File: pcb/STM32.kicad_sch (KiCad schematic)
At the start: 4 parts, among them CN1 Conn_02x08_Odd_Even, CN2 Conn_02x15_Odd_Even, CN3 Conn_02x10_Odd_Even, CN4 Conn_02x17_Odd_Even

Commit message: Updated PCB
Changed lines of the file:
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@@
 (kicad_sch (version 20230121) (generator eeschema)
   (paper "A4")
+  (hierarchical_label "Endschalter_Hinten_MCU" (shape input) (at 72.39 105.41 180) (fields_autoplaced)
+    (effects (font (size 1.27 1.27)) (justify right))
+  )
+  (hierarchical_label "Abstandsmessung_MCU" (shape input) (at 72.39 82.55 180) (fields_autoplaced)
+    (effects (font (size 1.27 1.27)) (justify right))
+  )
+  (hierarchical_label "Windgeschwindigkeit_MCU" (shape input) (at 72.39 74.93 180) (fields_autoplaced)
+    (effects (font (size 1.27 1.27)) (justify right))
+  )
+  (hierarchical_label "IN2_MCU" (shape output) (at 72.39 93.98 180) (fields_autoplaced)
+    (effects (font (size 1.27 1.27)) (justify right))
+  )
+  (hierarchical_label "IN1_MCU" (shape output) (at 72.39 90.17 180) (fields_autoplaced)
+    (effects (font (size 1.27 1.27)) (justify right))
+  )
+  (hierarchical_label "IN3_MCU" (shape output) (at 72.39 97.79 180) (fields_autoplaced)
+    (effects (font (size 1.27 1.27)) (justify right))
+  )
+  (hierarchical_label "Endschalter_Vorne_MCU" (shape input) (at 72.39 101.6 180) (fields_autoplaced)
+    (effects (font (size 1.27 1.27)) (justify right))
+  )
+  (hierarchical_label "Windrichtung_MCU" (shape input) (at 72.39 78.74 180) (fields_autoplaced)
+    (effects (font (size 1.27 1.27)) (justify right))
+  )
+  (hierarchical_label "Drehzahl_Analog_OUT" (shape input) (at 72.39 109.22 180) (fields_autoplaced)
+    (effects (font (size 1.27 1.27)) (justify right))
+  )
+  (hierarchical_label "IN0_MCU" (shape output) (at 72.39 86.36 180) (fields_autoplaced)
+    (effects (font (size 1.27 1.27)) (justify right))
+  )
+  (hierarchical_label "Kraftmessung_MCU" (shape input) (at 72.39 71.12 180) (fields_autoplaced)
+    (effects (font (size 1.27 1.27)) (justify right))
+  )
   (symbol (lib_id "Connector_Generic:Conn_02x17_Odd_Even") (at 166.37 100.33 0) (unit 1)
     (in_bom yes) (on_board yes) (dnp no) (fields_autoplaced)

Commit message: updated pcb
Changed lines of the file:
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@@
+    (effects (font (size 1.27 1.27)) (justify right))
+  )
+  (hierarchical_label "UART_EN" (shape output) (at 72.39 129.54 180) (fields_autoplaced)
     (effects (font (size 1.27 1.27)) (justify right))
   )
   (hierarchical_label "Windgeschwindigkeit_MCU" (shape input) (at 72.39 74.93 180) (fields_autoplaced)
+    (effects (font (size 1.27 1.27)) (justify right))
+  )
+  (hierarchical_label "OUT2_MCU" (shape output) (at 72.39 116.84 180) (fields_autoplaced)
+    (effects (font (size 1.27 1.27)) (justify right))
+  )
+  (hierarchical_label "UART_RX" (shape input) (at 72.39 124.46 180) (fields_autoplaced)
     (effects (font (size 1.27 1.27)) (justify right))
   )
@@
     (effects (font (size 1.27 1.27)) (justify right))
   )
+  (hierarchical_label "OUT3_MCU" (shape output) (at 72.39 120.65 180) (fields_autoplaced)
+    (effects (font (size 1.27 1.27)) (justify right))
+  )
   (hierarchical_label "IN3_MCU" (shape output) (at 72.39 97.79 180) (fields_autoplaced)
+    (effects (font (size 1.27 1.27)) (justify right))
+  )
+  (hierarchical_label "OUT1_MCU" (shape output) (at 72.39 113.03 180) (fields_autoplaced)
     (effects (font (size 1.27 1.27)) (justify right))
   )
@@
     (effects (font (size 1.27 1.27)) (justify right))
   )
+  (hierarchical_label "Strommessung_MCU" (shape input) (at 72.39 132.08 180) (fields_autoplaced)
+    (effects (font (size 1.27 1.27)) (justify right))
+  )
+  (hierarchical_label "UART_TX" (shape output) (at 72.39 127 180) (fields_autoplaced)
+    (effects (font (size 1.27 1.27)) (justify right))
+  )
   (hierarchical_label "Windrichtung_MCU" (shape input) (at 72.39 78.74 180) (fields_autoplaced)
     (effects (font (size 1.27 1.27)) (justify right))
   )
-  (hierarchical_label "Drehzahl_Analog_OUT" (shape input) (at 72.39 109.22 180) (fields_autoplaced)
+  (hierarchical_label "Drehzahl_Analog_OUT" (shape output) (at 72.39 109.22 180) (fields_autoplaced)
     (effects (font (size 1.27 1.27)) (justify right))
   )

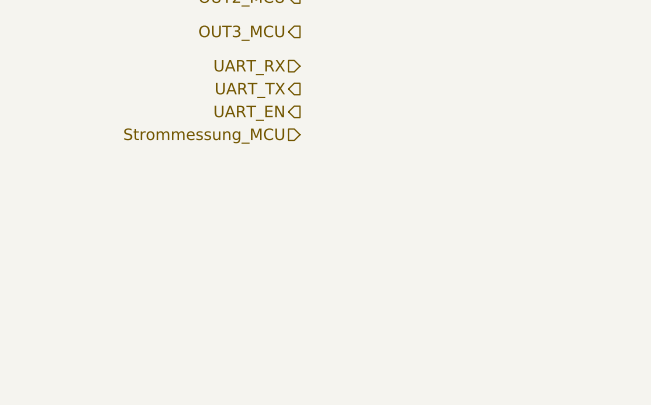
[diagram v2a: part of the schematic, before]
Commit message: added buttons & LEDs
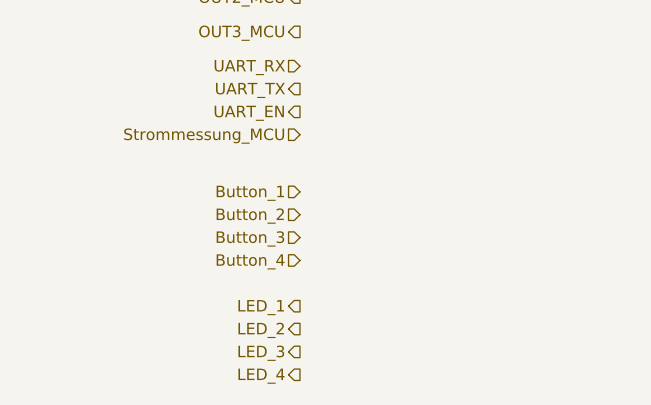
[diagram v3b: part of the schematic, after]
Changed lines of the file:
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@@
 (kicad_sch (version 20230121) (generator eeschema)
   (paper "A4")
+  (hierarchical_label "Button_1" (shape input) (at 72.39 138.43 180) (fields_autoplaced)
+    (effects (font (size 1.27 1.27)) (justify right))
+  )
   (hierarchical_label "Endschalter_Hinten_MCU" (shape input) (at 72.39 105.41 180) (fields_autoplaced)
+    (effects (font (size 1.27 1.27)) (justify right))
+  )
+  (hierarchical_label "Button_2" (shape input) (at 72.39 140.97 180) (fields_autoplaced)
     (effects (font (size 1.27 1.27)) (justify right))
   )
@@
     (effects (font (size 1.27 1.27)) (justify right))
   )
+  (hierarchical_label "LED_2" (shape output) (at 72.39 153.67 180) (fields_autoplaced)
+    (effects (font (size 1.27 1.27)) (justify right))
+  )
   (hierarchical_label "Windgeschwindigkeit_MCU" (shape input) (at 72.39 74.93 180) (fields_autoplaced)
+    (effects (font (size 1.27 1.27)) (justify right))
+  )
+  (hierarchical_label "LED_4" (shape output) (at 72.39 158.75 180) (fields_autoplaced)
     (effects (font (size 1.27 1.27)) (justify right))
   )
@@
     (effects (font (size 1.27 1.27)) (justify right))
   )
+  (hierarchical_label "Button_4" (shape input) (at 72.39 146.05 180) (fields_autoplaced)
+    (effects (font (size 1.27 1.27)) (justify right))
+  )
+  (hierarchical_label "LED_1" (shape output) (at 72.39 151.13 180) (fields_autoplaced)
+    (effects (font (size 1.27 1.27)) (justify right))
+  )
   (hierarchical_label "OUT1_MCU" (shape output) (at 72.39 113.03 180) (fields_autoplaced)
     (effects (font (size 1.27 1.27)) (justify right))
@@
     (effects (font (size 1.27 1.27)) (justify right))
   )
+  (hierarchical_label "Button_3" (shape input) (at 72.39 143.51 180) (fields_autoplaced)
+    (effects (font (size 1.27 1.27)) (justify right))
+  )
   (hierarchical_label "Windrichtung_MCU" (shape input) (at 72.39 78.74 180) (fields_autoplaced)
     (effects (font (size 1.27 1.27)) (justify right))
@@
     (effects (font (size 1.27 1.27)) (justify right))
   )
+  (hierarchical_label "LED_3" (shape output) (at 72.39 156.21 180) (fields_autoplaced)
+    (effects (font (size 1.27 1.27)) (justify right))
+  )

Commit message: Updated footprints
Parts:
- CN1: footprint (none) -> Connector_PinHeader_2.54mm:PinHeader_2x08_P2.54mm_Vertical_SMD
- CN2: footprint (none) -> Connector_PinHeader_2.54mm:PinHeader_2x15_P2.54mm_Vertical_SMD
- CN3: footprint (none) -> Connector_PinHeader_2.54mm:PinHeader_2x10_P2.54mm_Vertical_SMD
- CN4: footprint (none) -> Connector_PinHeader_2.54mm:PinHeader_2x17_P2.54mm_Vertical_SMD
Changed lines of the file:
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@@
     (effects (font (size 1.27 1.27)) (justify right))
   )
-  (hierarchical_label "OUT2_MCU" (shape output) (at 72.39 116.84 180) (fields_autoplaced)
+  (hierarchical_label "OUT2_MCU" (shape input) (at 72.39 116.84 180) (fields_autoplaced)
     (effects (font (size 1.27 1.27)) (justify right))
   )
@@
     (effects (font (size 1.27 1.27)) (justify right))
   )
-  (hierarchical_label "OUT3_MCU" (shape output) (at 72.39 120.65 180) (fields_autoplaced)
+  (hierarchical_label "OUT3_MCU" (shape input) (at 72.39 120.65 180) (fields_autoplaced)
     (effects (font (size 1.27 1.27)) (justify right))
   )
@@
     (effects (font (size 1.27 1.27)) (justify right))
   )
-  (hierarchical_label "OUT1_MCU" (shape output) (at 72.39 113.03 180) (fields_autoplaced)
+  (hierarchical_label "OUT1_MCU" (shape input) (at 72.39 113.03 180) (fields_autoplaced)
     (effects (font (size 1.27 1.27)) (justify right))
   )
@@
       (effects (font (size 1.27 1.27)))
     )
-    (property "Footprint" "" (at 166.37 100.33 0)
+    (property "Footprint" "Connector_PinHeader_2.54mm:PinHeader_2x17_P2.54mm_Vertical_SMD" (at 166.37 100.33 0)
       (effects (font (size 1.27 1.27)) hide)
     )
@@
       (effects (font (size 1.27 1.27)))
     )
-    (property "Footprint" "" (at 142.24 55.88 0)
+    (property "Footprint" "Connector_PinHeader_2.54mm:PinHeader_2x08_P2.54mm_Vertical_SMD" (at 142.24 55.88 0)
       (effects (font (size 1.27 1.27)) hide)
     )
@@
       (effects (font (size 1.27 1.27)))
     )
-    (property "Footprint" "" (at 166.37 58.42 0)
+    (property "Footprint" "Connector_PinHeader_2.54mm:PinHeader_2x10_P2.54mm_Vertical_SMD" (at 166.37 58.42 0)
       (effects (font (size 1.27 1.27)) hide)
     )
@@
       (effects (font (size 1.27 1.27)))
     )
-    (property "Footprint" "" (at 142.24 92.71 0)
-      (effects (font (size 1.27 1.27)) hide)
-    )
+    (property "Footprint" "Connector_PinHeader_2.54mm:PinHeader_2x15_P2.54mm_Vertical_SMD" (at 142.24 92.71 0)
+      (effects (font (size 1.27 1.27)) hide)
+    )

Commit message: Save pcb cut out
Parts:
- CN1: footprint Connector_PinHeader_2.54mm:PinHeader_2x08_P2.54mm_Vertical_SMD -> Connector_PinHeader_2.54mm:PinHeader_2x08_P2.54mm_Vertical
- CN2: footprint Connector_PinHeader_2.54mm:PinHeader_2x15_P2.54mm_Vertical_SMD -> Connector_PinHeader_2.54mm:PinHeader_2x15_P2.54mm_Vertical
- CN3: footprint Connector_PinHeader_2.54mm:PinHeader_2x10_P2.54mm_Vertical_SMD -> Connector_PinHeader_2.54mm:PinHeader_2x10_P2.54mm_Vertical
- CN4: footprint Connector_PinHeader_2.54mm:PinHeader_2x17_P2.54mm_Vertical_SMD -> Connector_PinHeader_2.54mm:PinHeader_2x17_P2.54mm_Vertical
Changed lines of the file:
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@@
       (effects (font (size 1.27 1.27)))
     )
-    (property "Footprint" "Connector_PinHeader_2.54mm:PinHeader_2x17_P2.54mm_Vertical_SMD" (at 166.37 100.33 0)
+    (property "Footprint" "Connector_PinHeader_2.54mm:PinHeader_2x17_P2.54mm_Vertical" (at 166.37 100.33 0)
       (effects (font (size 1.27 1.27)) hide)
     )
@@
         )
         (path "/19bff231-ff37-4a40-bd06-2039e9f55c77/9c6dbdee-9d8a-4cc8-8ceb-3d83c2e63e3b"
-          (reference "CN4") (unit 1)
+          (reference "CN10") (unit 1)
         )
       )
@@
       (effects (font (size 1.27 1.27)))
     )
-    (property "Footprint" "Connector_PinHeader_2.54mm:PinHeader_2x08_P2.54mm_Vertical_SMD" (at 142.24 55.88 0)
+    (property "Footprint" "Connector_PinHeader_2.54mm:PinHeader_2x08_P2.54mm_Vertical" (at 142.24 55.88 0)
       (effects (font (size 1.27 1.27)) hide)
     )
@@
         )
         (path "/19bff231-ff37-4a40-bd06-2039e9f55c77/9c6dbdee-9d8a-4cc8-8ceb-3d83c2e63e3b"
-          (reference "CN1") (unit 1)
+          (reference "CN8") (unit 1)
         )
       )
@@
       (effects (font (size 1.27 1.27)))
     )
-    (property "Footprint" "Connector_PinHeader_2.54mm:PinHeader_2x10_P2.54mm_Vertical_SMD" (at 166.37 58.42 0)
+    (property "Footprint" "Connector_PinHeader_2.54mm:PinHeader_2x10_P2.54mm_Vertical" (at 166.37 58.42 0)
       (effects (font (size 1.27 1.27)) hide)
     )
@@
         )
         (path "/19bff231-ff37-4a40-bd06-2039e9f55c77/9c6dbdee-9d8a-4cc8-8ceb-3d83c2e63e3b"
-          (reference "CN3") (unit 1)
+          (reference "CN7") (unit 1)
         )
       )
@@
       (effects (font (size 1.27 1.27)))
     )
-    (property "Footprint" "Connector_PinHeader_2.54mm:PinHeader_2x15_P2.54mm_Vertical_SMD" (at 142.24 92.71 0)
+    (property "Footprint" "Connector_PinHeader_2.54mm:PinHeader_2x15_P2.54mm_Vertical" (at 142.24 92.71 0)
       (effects (font (size 1.27 1.27)) hide)
     )
@@
         )
         (path "/19bff231-ff37-4a40-bd06-2039e9f55c77/9c6dbdee-9d8a-4cc8-8ceb-3d83c2e63e3b"
-          (reference "CN2") (unit 1)
+          (reference "CN9") (unit 1)
         )
       )

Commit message: updated pcb
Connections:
- net Abstandsmessung_MCU: now also CN4.30 (Pin_30)
- net Button_1: now also CN4.2 (Pin_2)
- net Button_2: now also CN4.4 (Pin_4)
- net Button_3: now also CN4.8 (Pin_8)
- net Button_4: now also CN4.6 (Pin_6)
- net Drehzahl_Analog_OUT: now also CN3.18 (Pin_18)
- net Endschalter_Hinten_MCU: now also CN3.4 (Pin_4)
- net Endschalter_Vorne_MCU: now also CN3.1 (Pin_1)
- net IN0_MCU: now also CN3.3 (Pin_3)
- net IN1_MCU: now also CN3.2 (Pin_2)
- net IN2_MCU: now also CN1.11 (Pin_11)
- net IN3_MCU: now also CN1.9 (Pin_9)
- net Kraftmessung_MCU: now also CN4.32 (Pin_32)
- net LED_1: now also CN4.10 (Pin_10)
- net LED_2: now also CN4.12 (Pin_12)
- net LED_3: now also CN4.14 (Pin_14)
- net LED_4: now also CN4.16 (Pin_16)
- net OUT1_MCU: now also CN1.3 (Pin_3)
- net OUT2_MCU: now also CN1.5 (Pin_5)
- net OUT3_MCU: now also CN1.7 (Pin_7)
- net Strommessung_MCU: now also CN2.16 (Pin_16)
- net UART_EN: now also CN2.3 (Pin_3)
- net UART_RX: now also CN2.2 (Pin_2)
- net UART_TX: now also CN2.5 (Pin_5)
- net Windgeschwindigkeit_MCU: now also CN2.27 (Pin_27)
- net Windrichtung_MCU: now also CN2.25 (Pin_25)
- net LED_5: now reaches CN4.18 (Pin_18)
- net LED_6: now reaches CN4.20 (Pin_20)
- net LED_7: now reaches CN4.22 (Pin_22)
- net ext_Relais_1: now reaches CN4.33 (Pin_33)
- net ext_Relais_2: now reaches CN4.34 (Pin_34)
- net +3.3V: now reaches CN1.8 (Pin_8)
- net Opt_Analog_IN: now reaches CN3.11 (Pin_11)
- net Opt_Temperaturmessung: now reaches CN3.9 (Pin_9)
- no-connect marks 0 -> 66
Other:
- moved on the sheet: CN1, CN2

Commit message: finished PCB Design V1.0
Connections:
- net Button_1: now also CN3.20 (Pin_20); no longer CN4.2 (Pin_2)
- net Button_2: now also CN4.2 (Pin_2); no longer CN4.4 (Pin_4)
- net Button_3: now also CN4.6 (Pin_6); no longer CN4.8 (Pin_8)
- net Button_4: now also CN4.4 (Pin_4); no longer CN4.6 (Pin_6)
- net LED_1: now also CN4.8 (Pin_8); no longer CN4.10 (Pin_10)
- net LED_2: now also CN4.10 (Pin_10); no longer CN4.12 (Pin_12)
- net LED_3: now also CN4.12 (Pin_12); no longer CN4.14 (Pin_14)
- net LED_4: now also CN4.14 (Pin_14); no longer CN4.16 (Pin_16)
- net LED_5: now also CN4.16 (Pin_16); no longer CN4.18 (Pin_18)
- net LED_6: now also CN4.15 (Pin_15); no longer CN4.20 (Pin_20)
- net LED_7: now also CN4.17 (Pin_17); no longer CN4.22 (Pin_22)
